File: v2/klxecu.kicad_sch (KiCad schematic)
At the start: 14 parts, among them J1 CAM_SENSOR_IN, J2 Conn_01x06, U1 S36B-WPZK-A, U2 LM2940S-5.0/NOPB, U3 Arduino Mega 2560 Pro

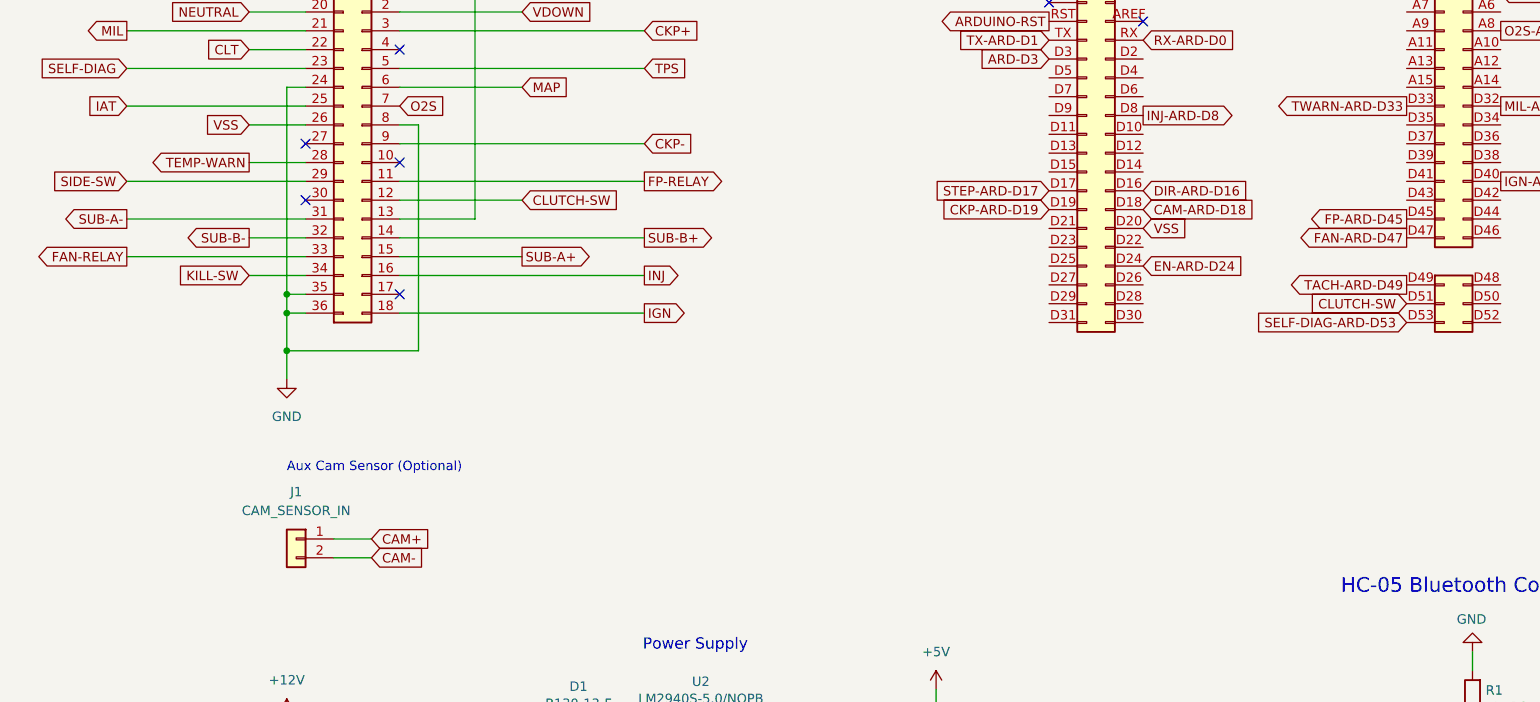
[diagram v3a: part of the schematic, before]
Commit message: Add control of air switching valve
Plus a jumper to lock the valve closed
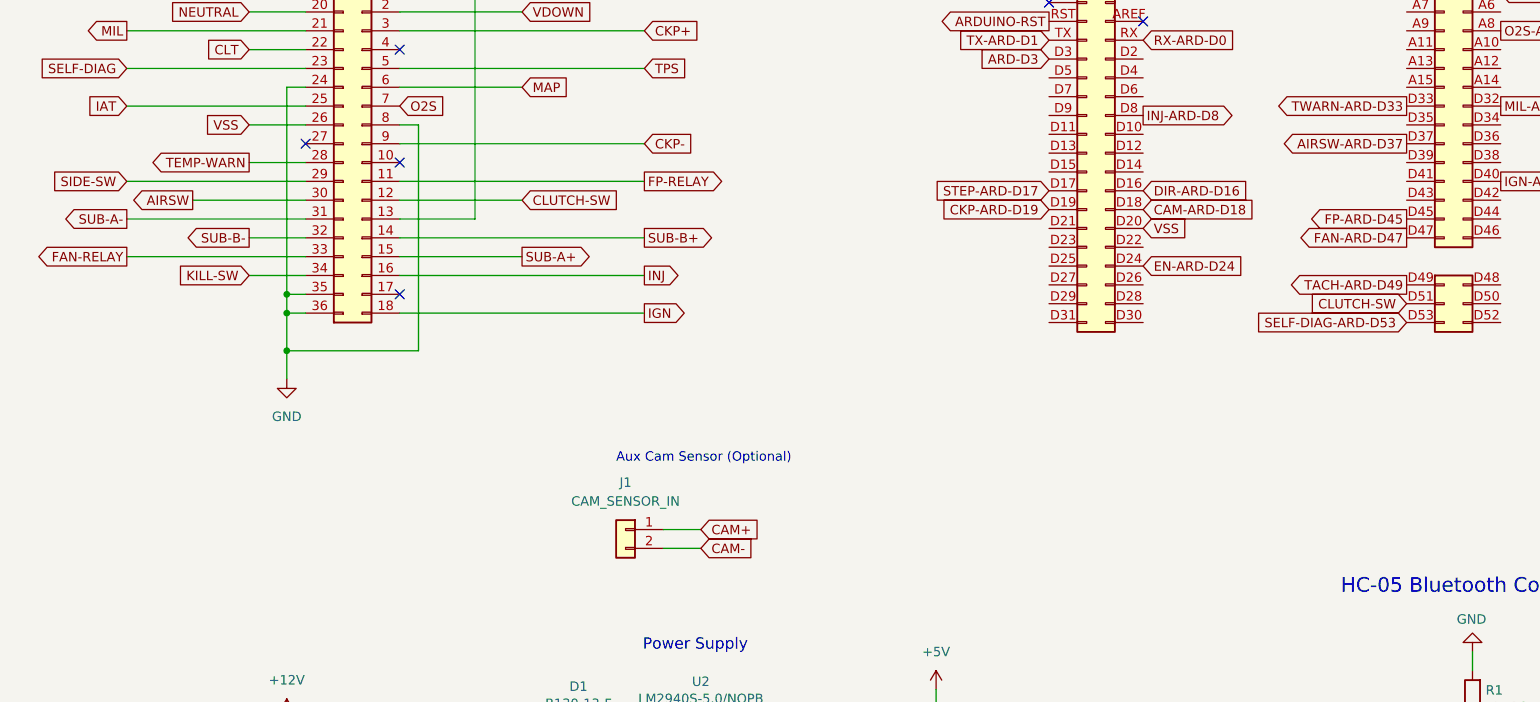
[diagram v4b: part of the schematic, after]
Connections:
- net AIRSW: now reaches U1.30
- net AIRSW-ARD-D37: now reaches U3.D37
- no-connect marks 9 -> 8
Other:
- moved on the sheet: J1
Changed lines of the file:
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@@
   (no_connect (at 158.75 34.29))
   (no_connect (at 58.42 53.34))
-  (no_connect (at 58.42 60.96))
   (no_connect (at 71.12 40.64))
   (wire (pts (xy 90.17 146.05) (xy 90.17 148.59))
@@
     (stroke (width 0) (type default) (color 0 0 0 0))
   )
-  (wire (pts (xy 62.23 106.68) (xy 67.31 106.68))
+  (wire (pts (xy 106.68 105.41) (xy 111.76 105.41))
     (stroke (width 0) (type default) (color 0 0 0 0))
   )
@@
     (stroke (width 0) (type default) (color 0 0 0 0))
   )
-  (wire (pts (xy 62.23 109.22) (xy 67.31 109.22))
+  (wire (pts (xy 106.68 107.95) (xy 111.76 107.95))
     (stroke (width 0) (type default) (color 0 0 0 0))
   )
@@
     (stroke (width 0) (type default) (color 0 0 0 0))
   )
+  (wire (pts (xy 43.18 60.96) (xy 58.42 60.96))
+    (stroke (width 0) (type default) (color 0 0 0 0))
+  )
   (wire (pts (xy 55.88 138.43) (xy 64.77 138.43))
     (stroke (width 0) (type default) (color 0 0 0 0))
@@
     (stroke (width 0) (type default) (color 0 0 0 0))
   )
-  (text "Aux Cam Sensor (Optional)\n" (at 55.88 97.79 0)
+  (text "Aux Cam Sensor (Optional)\n" (at 100.33 96.52 0)
     (effects (font (size 1.27 1.27)) (justify left bottom))
   )
@@
     )
   )
-  (global_label "CAM+" (shape input) (at 67.31 106.68 0) (fields_autoplaced)
-    (effects (font (size 1.27 1.27)) (justify left))
-    (property "Intersheet References" "${INTERSHEET_REFS}" (id 0) (at 75.1055 106.6006 0)
+  (global_label "CAM+" (shape input) (at 111.76 105.41 0) (fields_autoplaced)
+    (effects (font (size 1.27 1.27)) (justify left))
+    (property "Intersheet References" "${INTERSHEET_REFS}" (id 0) (at 119.5555 105.3306 0)
       (effects (font (size 1.27 1.27)) (justify left) hide)
     )
@@
     )
   )
-  (global_label "CAM-" (shape input) (at 67.31 109.22 0) (fields_autoplaced)
-    (effects (font (size 1.27 1.27)) (justify left))
-    (property "Intersheet References" "${INTERSHEET_REFS}" (id 0) (at 75.1055 109.1406 0)
+  (global_label "CAM-" (shape input) (at 111.76 107.95 0) (fields_autoplaced)
+    (effects (font (size 1.27 1.27)) (justify left))
+    (property "Intersheet References" "${INTERSHEET_REFS}" (id 0) (at 119.5555 107.8706 0)
       (effects (font (size 1.27 1.27)) (justify left) hide)
     )
@@
     )
   )
+  (global_label "AIRSW" (shape output) (at 43.18 60.96 180) (fields_autoplaced)
+    (effects (font (size 1.27 1.27)) (justify right))
+    (property "Intersheet References" "${INTERSHEET_REFS}" (id 0) (at 35.1426 61.0394 0)
+      (effects (font (size 1.27 1.27)) (justify right) hide)
+    )
+  )
   (global_label "MAP" (shape input) (at 87.63 45.72 0) (fields_autoplaced)
     (effects (font (size 1.27 1.27)) (justify left))
@@
     (effects (font (size 1.27 1.27)) (justify right))
     (property "Intersheet References" "${INTERSHEET_REFS}" (id 0) (at 193.1669 75.0094 0)
+      (effects (font (size 1.27 1.27)) (justify right) hide)
+    )
+  )
+  (global_label "AIRSW-ARD-D37" (shape output) (at 207.01 53.34 180) (fields_autoplaced)
+    (effects (font (size 1.27 1.27)) (justify right))
+    (property "Intersheet References" "${INTERSHEET_REFS}" (id 0) (at 188.5102 53.2606 0)
       (effects (font (size 1.27 1.27)) (justify right) hide)
     )
@@
     (pin "3")
   )
-  (symbol (lib_id "Connector_Generic:Conn_01x02") (at 57.15 106.68 0) (mirror y) (unit 1)
+  (symbol (lib_id "Connector_Generic:Conn_01x02") (at 101.6 105.41 0) (mirror y) (unit 1)
     (in_bom yes) (on_board yes)
-    (property "Reference" "J1" (id 0) (at 57.15 100.33 0))
-    (property "Value" "CAM_SENSOR_IN" (id 1) (at 57.15 102.87 0))
-    (property "Footprint" "Connector_PinHeader_2.54mm:PinHeader_1x02_P2.54mm_Vertical" (id 2) (at 57.15 106.68 0)
-      (effects (font (size 1.27 1.27)) hide)
-    )
-    (property "Datasheet" "~" (id 3) (at 57.15 106.68 0)
+    (property "Reference" "J1" (id 0) (at 101.6 99.06 0))
+    (property "Value" "CAM_SENSOR_IN" (id 1) (at 101.6 101.6 0))
+    (property "Footprint" "Connector_PinHeader_2.54mm:PinHeader_1x02_P2.54mm_Vertical" (id 2) (at 101.6 105.41 0)
+      (effects (font (size 1.27 1.27)) hide)
+    )
+    (property "Datasheet" "~" (id 3) (at 101.6 105.41 0)
       (effects (font (size 1.27 1.27)) hide)
     )
@@
       (reference "#PWR023") (unit 1) (value "GND") (footprint "")
     )
+    (path "/98f72596-e058-4dba-8464-025a303cdc65/ba3a3e4f-d4a5-47f8-af26-edcfc7202ede"
+      (reference "#PWR024") (unit 1) (value "GND") (footprint "")
+    )
     (path "/98f72596-e058-4dba-8464-025a303cdc65/da4f1a5f-5f0b-4fe5-854c-ac5a3ad70437"
       (reference "#PWR025") (unit 1) (value "GND") (footprint "")
@@
       (reference "#PWR047") (unit 1) (value "GND") (footprint "")
     )
-    (path "/98f72596-e058-4dba-8464-025a303cdc65/ba3a3e4f-d4a5-47f8-af26-edcfc7202ede"
-      (reference "#PWR?") (unit 1) (value "GND") (footprint "")
+    (path "/a01c941e-2669-451e-92d9-4d3556674fec/91001002-c72f-4bbf-b741-bf3072d0f610"
+      (reference "#PWR048") (unit 1) (value "GND") (footprint "")
     )
     (path "/a01c941e-2669-451e-92d9-4d3556674fec/75126fec-323d-4a00-8d28-b0141aa312d7"
@@
       (reference "C13") (unit 1) (value "100nF") (footprint "Capacitor_SMD:C_0805_2012Metric_Pad1.18x1.45mm_HandSolder")
     )
+    (path "/98f72596-e058-4dba-8464-025a303cdc65/db86639b-6847-44b0-bd56-1d0ca68cc2d0"
+      (reference "C14") (unit 1) (value "100nF") (footprint "Capacitor_SMD:C_0805_2012Metric_Pad1.18x1.45mm_HandSolder")
+    )
     (path "/98f72596-e058-4dba-8464-025a303cdc65/f90580b8-7957-4d84-a27f-4a384f7f00f9"
       (reference "C15") (unit 1) (value "100nF") (footprint "Capacitor_SMD:C_0805_2012Metric_Pad1.18x1.45mm_HandSolder")
@@
       (reference "C16") (unit 1) (value "0.33uF") (footprint "Capacitor_SMD:C_0805_2012Metric_Pad1.18x1.45mm_HandSolder")
     )
+    (path "/98f72596-e058-4dba-8464-025a303cdc65/836826c5-a09c-468c-b76a-db846e15572a"
+      (reference "C17") (unit 1) (value "0.33uF") (footprint "Capacitor_SMD:C_0805_2012Metric_Pad1.18x1.45mm_HandSolder")
+    )
     (path "/98f72596-e058-4dba-8464-025a303cdc65/65d2aec2-bb44-4c35-b65c-24c7742f9fcc"
       (reference "C18") (unit 1) (value "0.22uF") (footprint "Capacitor_SMD:C_0805_2012Metric_Pad1.18x1.45mm_HandSolder")
@@
       (reference "C21") (unit 1) (value "100uF") (footprint "Capacitor_THT:CP_Radial_D5.0mm_P2.50mm")
     )
-    (path "/98f72596-e058-4dba-8464-025a303cdc65/836826c5-a09c-468c-b76a-db846e15572a"
-      (reference "C?") (unit 1) (value "0.33uF") (footprint "Capacitor_SMD:C_0805_2012Metric_Pad1.18x1.45mm_HandSolder")
-    )
-    (path "/98f72596-e058-4dba-8464-025a303cdc65/db86639b-6847-44b0-bd56-1d0ca68cc2d0"
-      (reference "C?") (unit 1) (value "100nF") (footprint "Capacitor_SMD:C_0805_2012Metric_Pad1.18x1.45mm_HandSolder")
-    )
     (path "/f8dcc113-360c-4a3f-b3ce-db2657bf4383"
       (reference "D1") (unit 1) (value "B130-13-F") (footprint "Diode_SMD:D_SMA")
@@
       (reference "JP1") (unit 1) (value "Jumper_3_Open") (footprint "Connector_PinHeader_2.54mm:PinHeader_1x03_P2.54mm_Vertical")
     )
+    (path "/a01c941e-2669-451e-92d9-4d3556674fec/812391a2-bda3-4c6e-9436-4b9a4185829a"
+      (reference "JP2") (unit 1) (value "Jumper_2_Open") (footprint "Connector_PinHeader_2.54mm:PinHeader_1x02_P2.54mm_Vertical")
+    )
     (path "/a01c941e-2669-451e-92d9-4d3556674fec/a246c3a3-766a-4abe-89a4-b39b374a1baf"
       (reference "Q1") (unit 1) (value "SSM3K357R") (footprint "Package_TO_SOT_SMD:SOT-23")
@@
       (reference "Q6") (unit 1) (value "SSM3K357R") (footprint "Package_TO_SOT_SMD:SOT-23")
     )
+    (path "/a01c941e-2669-451e-92d9-4d3556674fec/53b25b36-64a3-4815-a74c-60fbd4a5e8c6"
+      (reference "Q7") (unit 1) (value "SSM3K357R") (footprint "Package_TO_SOT_SMD:SOT-23")
+    )
     (path "/a922357b-c635-425c-83b6-ff0a5ae36fb8"
       (reference "R1") (unit 1) (value "2k") (footprint "Resistor_SMD:R_0805_2012Metric")
@@
       (reference "R12") (unit 1) (value "470") (footprint "Resistor_SMD:R_0805_2012Metric_Pad1.20x1.40mm_HandSolder")
     )
+    (path "/98f72596-e058-4dba-8464-025a303cdc65/1b734947-4591-44d6-ba02-cd89adc71133"
+      (reference "R13") (unit 1) (value "470") (footprint "Resistor_SMD:R_0805_2012Metric_Pad1.20x1.40mm_HandSolder")
+    )
     (path "/98f72596-e058-4dba-8464-025a303cdc65/7ba465b4-7f8f-4502-ab04-134cac56c7c6"
       (reference "R14") (unit 1) (value "470") (footprint "Resistor_SMD:R_0805_2012Metric_Pad1.20x1.40mm_HandSolder")
@@
       (reference "R21") (unit 1) (value "10K") (footprint "Resistor_SMD:R_0805_2012Metric")
     )
-    (path "/98f72596-e058-4dba-8464-025a303cdc65/1b734947-4591-44d6-ba02-cd89adc71133"
-      (reference "R?") (unit 1) (value "470") (footprint "Resistor_SMD:R_0805_2012Metric_Pad1.20x1.40mm_HandSolder")
-    )
     (path "/e7efca28-0eae-4ec9-be91-e1da3a3f1517"
